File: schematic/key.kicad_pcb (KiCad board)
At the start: 2 copper layers, 7 parts

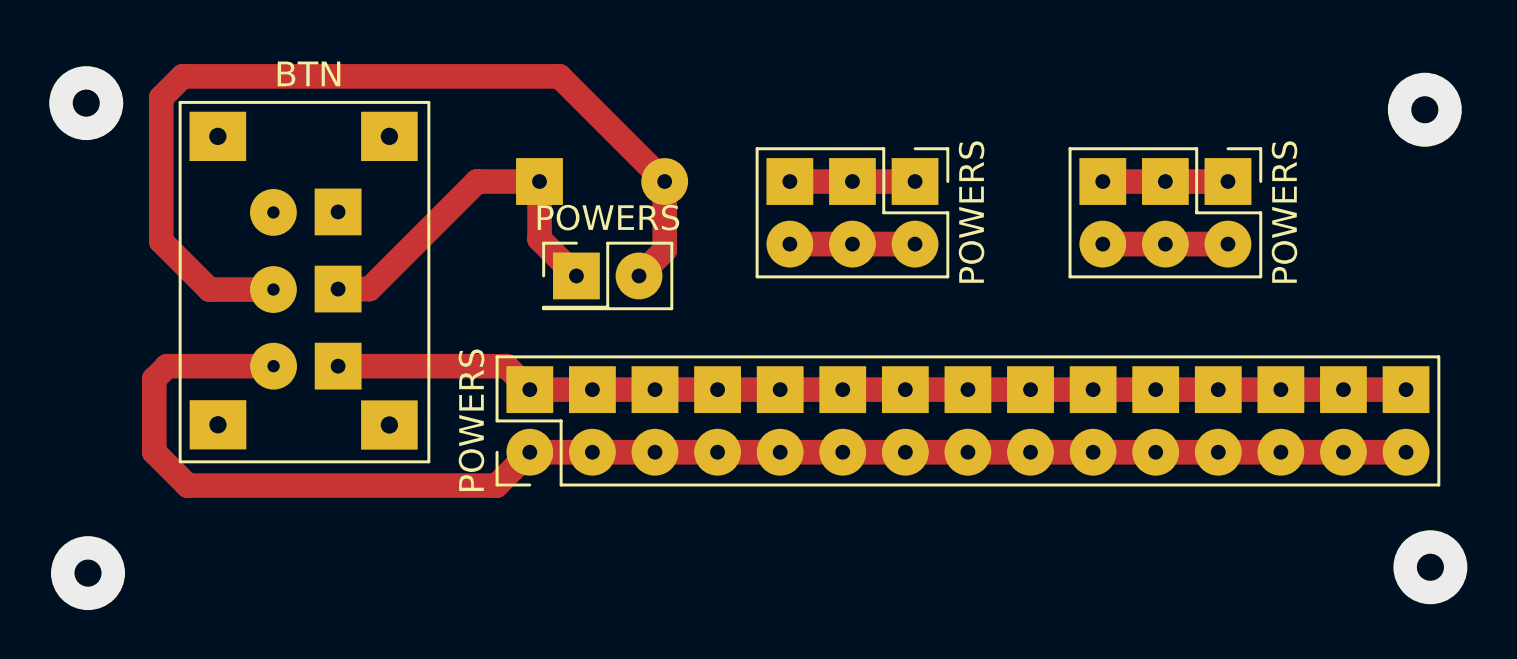
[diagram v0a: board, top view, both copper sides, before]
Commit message: New button board
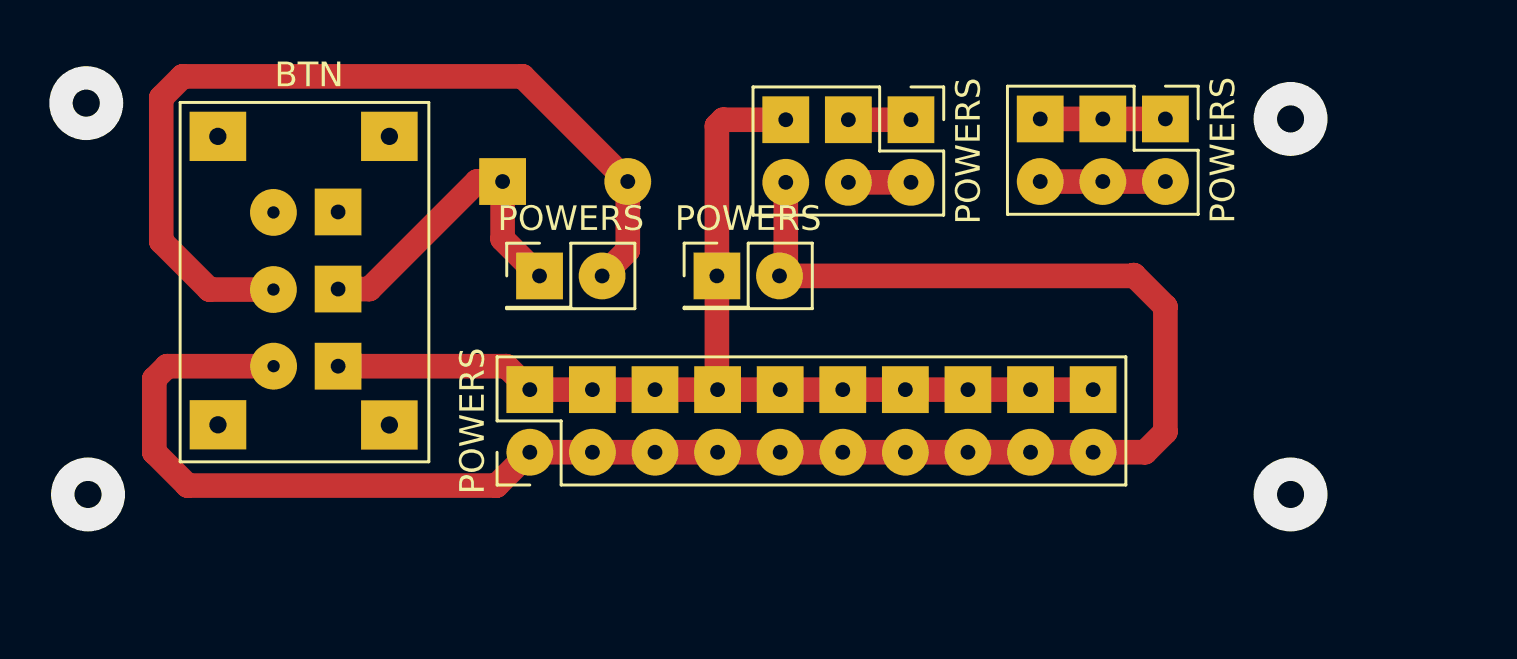
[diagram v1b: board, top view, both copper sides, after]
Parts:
- added POWERS: POWERS, Connector_PinHeader_2.54mm:PinHeader_2x01_P2.54mm_Vertical, F.Cu at (40.2, 21.6)
- POWERS: footprint Connector_PinHeader_2.54mm:PinHeader_2x15_P2.54mm_Vertical -> Connector_PinHeader_2.54mm:PinHeader_2x10_P2.54mm_Vertical
- moved POWERS 3.59 mm to (58.4, 15.2)
- moved POWERS 2.51 mm to (48.1, 15.3)
- moved ? 1.50 mm to (31.5, 17.8)
- moved ? 1.50 mm to (36.6, 17.8)
- moved POWERS 1.50 mm to (33.0, 21.6)
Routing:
- net (no net): track 176.5 -> 185.1 mm
